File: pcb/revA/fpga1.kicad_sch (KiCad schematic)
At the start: 21 parts, among them U1 XC6SLX25-FTG256

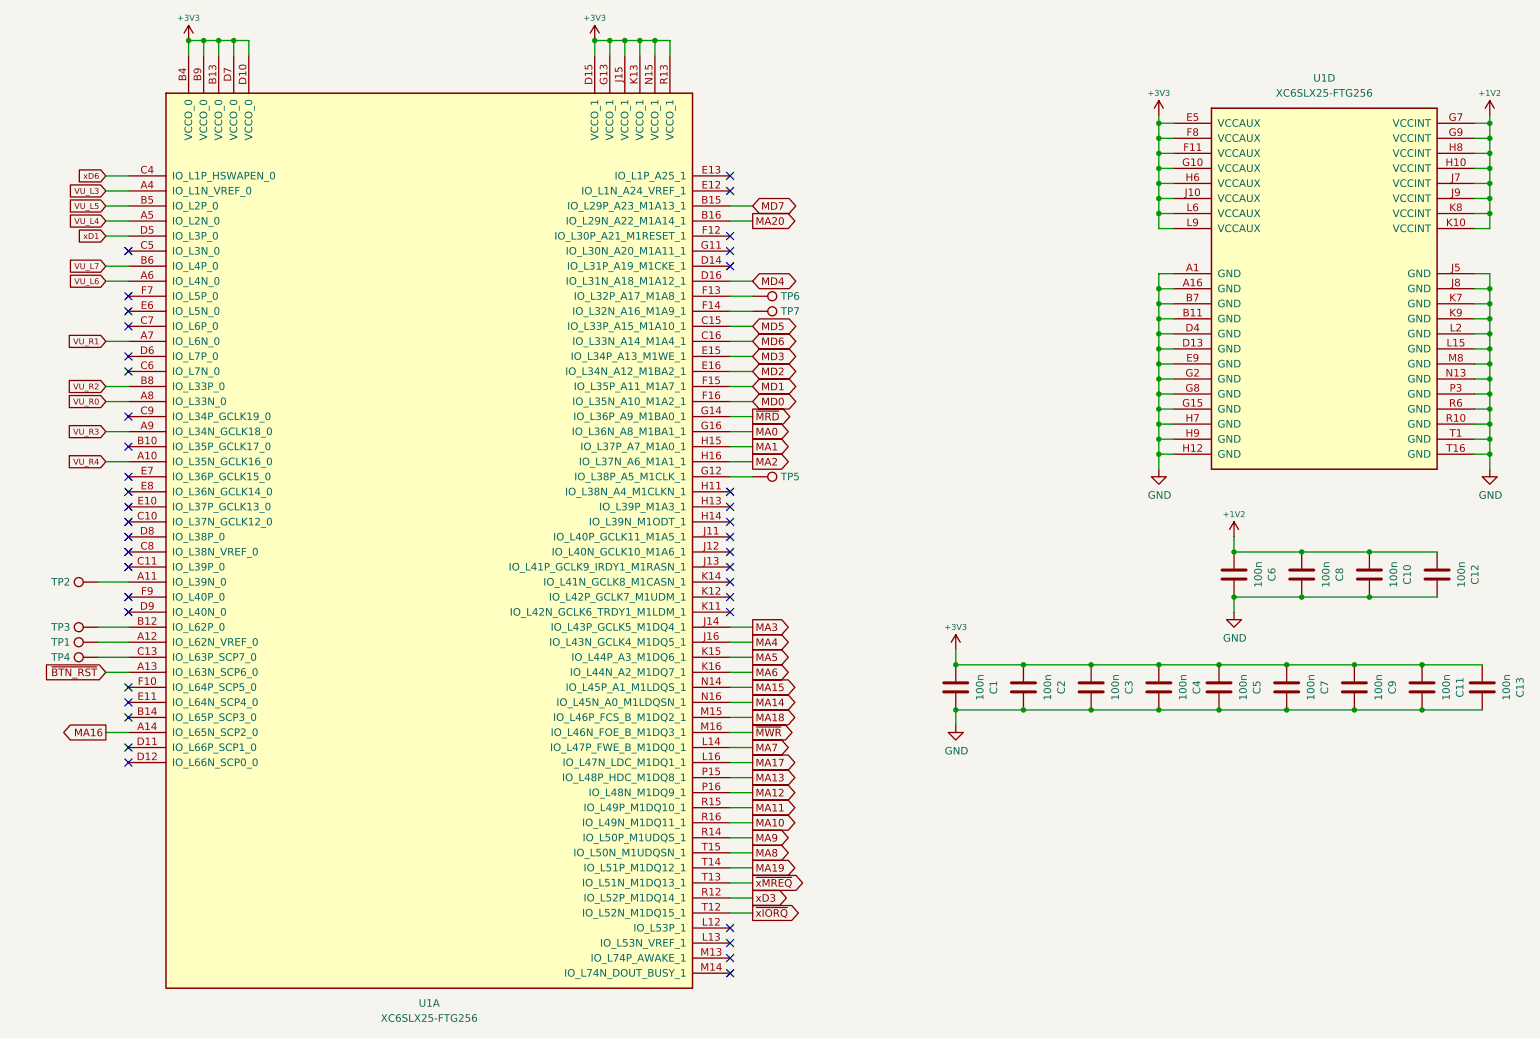
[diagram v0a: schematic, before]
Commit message: Updated gerbers to min 0.2/0.45 vias, firmware build for xc6slx16
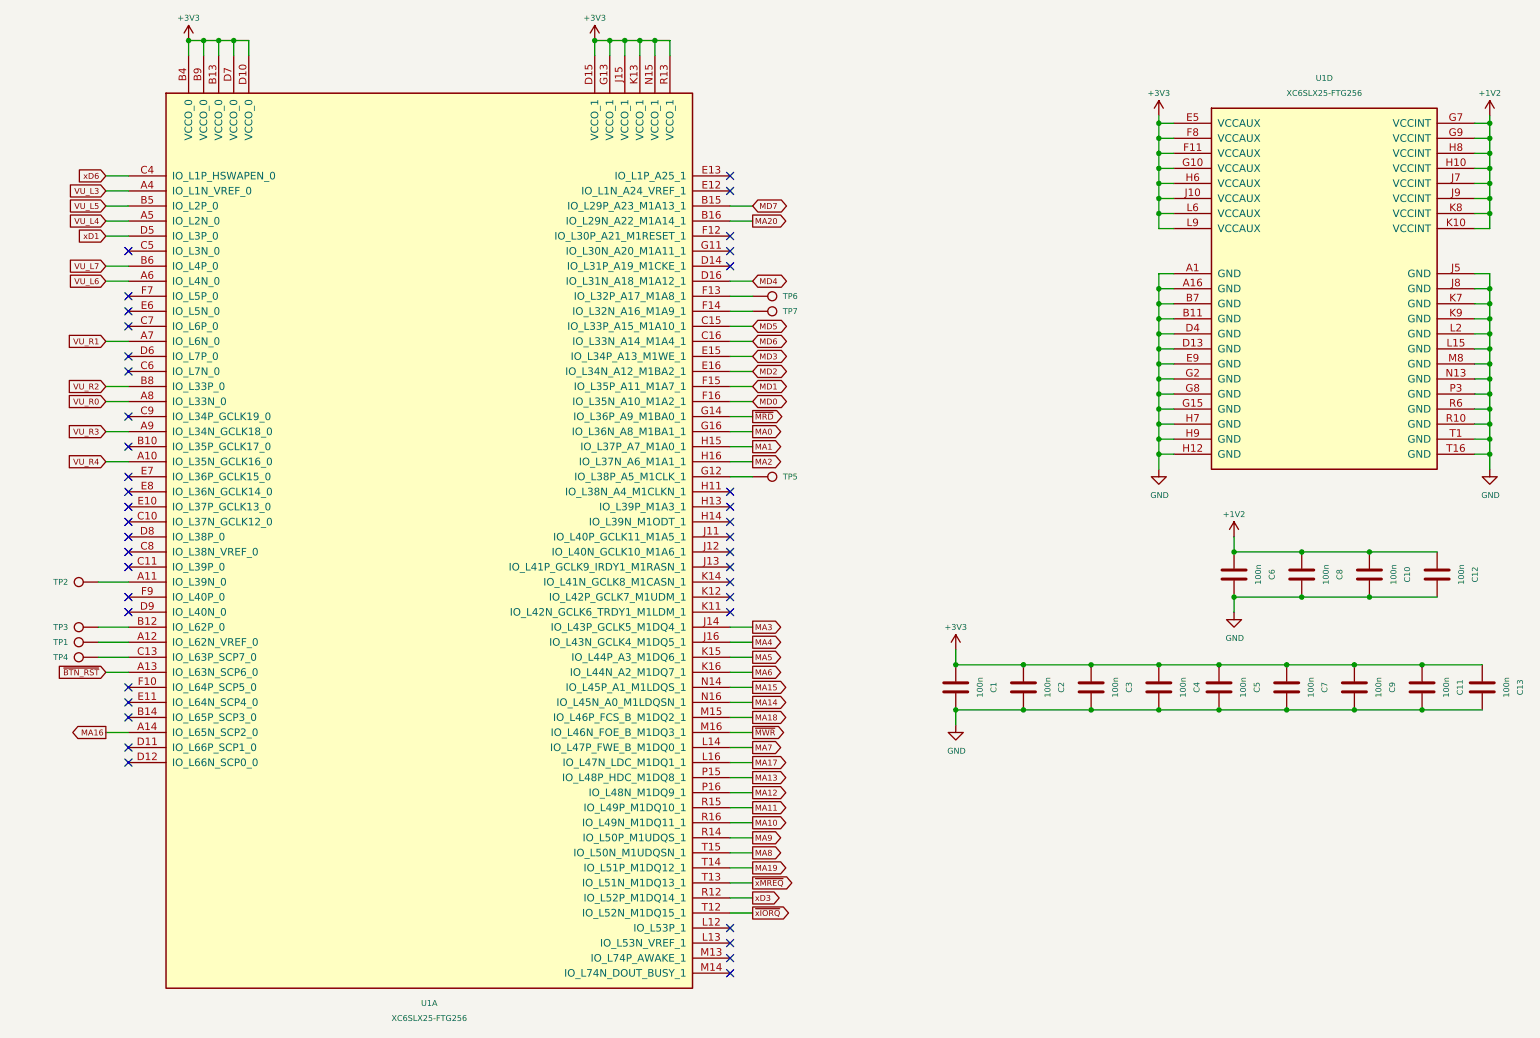
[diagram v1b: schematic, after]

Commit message: Updated revA (cosmetic changes)
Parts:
- TP1, TP2, TP3, TP4, TP5, TP6, TP7: now left out of the parts list
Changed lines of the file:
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@@
 		(body_style 1)
 		(exclude_from_sim no)
-		(in_bom yes)
+		(in_bom no)
 		(on_board yes)
 		(in_pos_files yes)
@@
 		(body_style 1)
 		(exclude_from_sim no)
-		(in_bom yes)
+		(in_bom no)
 		(on_board yes)
 		(in_pos_files yes)
@@
 		(body_style 1)
 		(exclude_from_sim no)
-		(in_bom yes)
+		(in_bom no)
 		(on_board yes)
 		(in_pos_files yes)
@@
 		(body_style 1)
 		(exclude_from_sim no)
-		(in_bom yes)
+		(in_bom no)
 		(on_board yes)
 		(in_pos_files yes)
@@
 		(body_style 1)
 		(exclude_from_sim no)
-		(in_bom yes)
+		(in_bom no)
 		(on_board yes)
 		(in_pos_files yes)
@@
 		(body_style 1)
 		(exclude_from_sim no)
-		(in_bom yes)
+		(in_bom no)
 		(on_board yes)
 		(in_pos_files yes)
@@
 		(body_style 1)
 		(exclude_from_sim no)
-		(in_bom yes)
+		(in_bom no)
 		(on_board yes)
 		(in_pos_files yes)
